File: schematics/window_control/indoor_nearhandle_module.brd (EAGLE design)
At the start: 54.6 x 59.4 mm, 19 parts, among them J1 J2, J2 J2, Q1 2N3904, SW1 MRS-101-2C3-B, U1 ESP32, U4 SN74LS32N

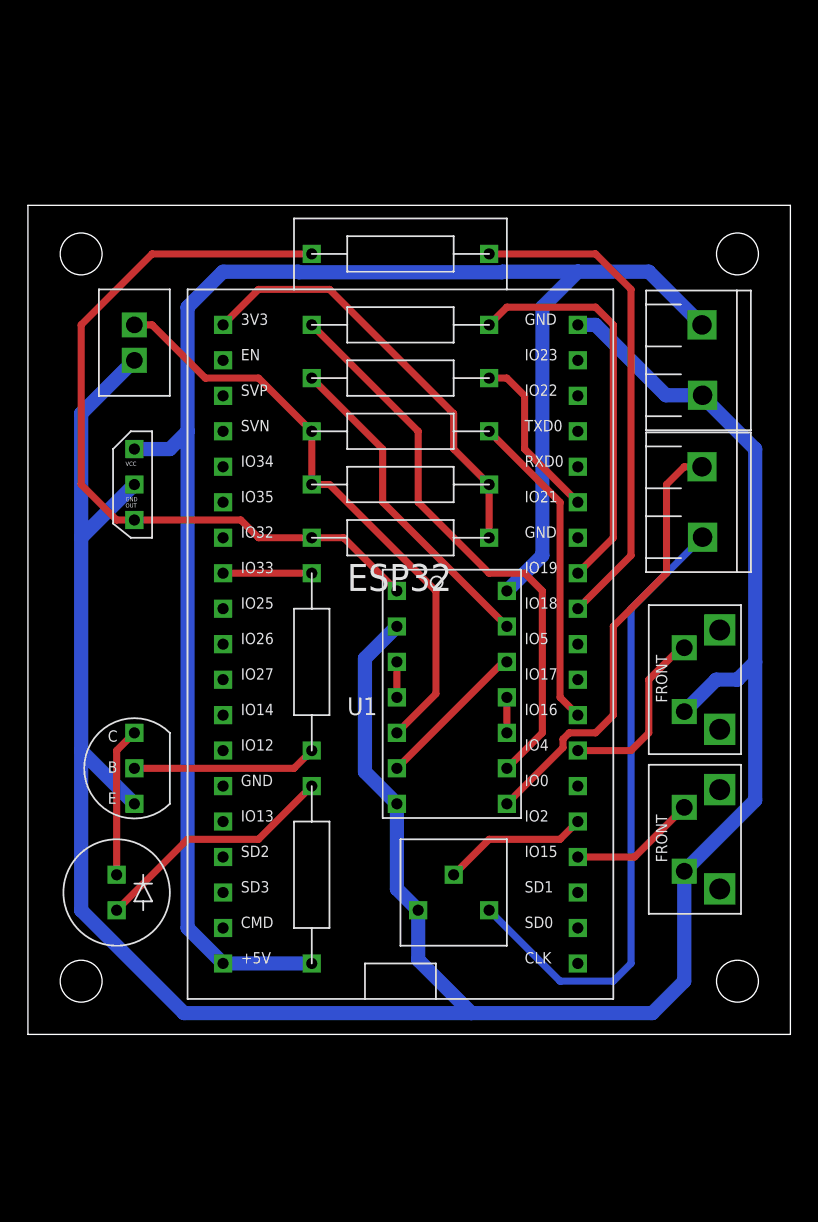
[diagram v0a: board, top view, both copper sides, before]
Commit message: Board redesigned to reduce it width
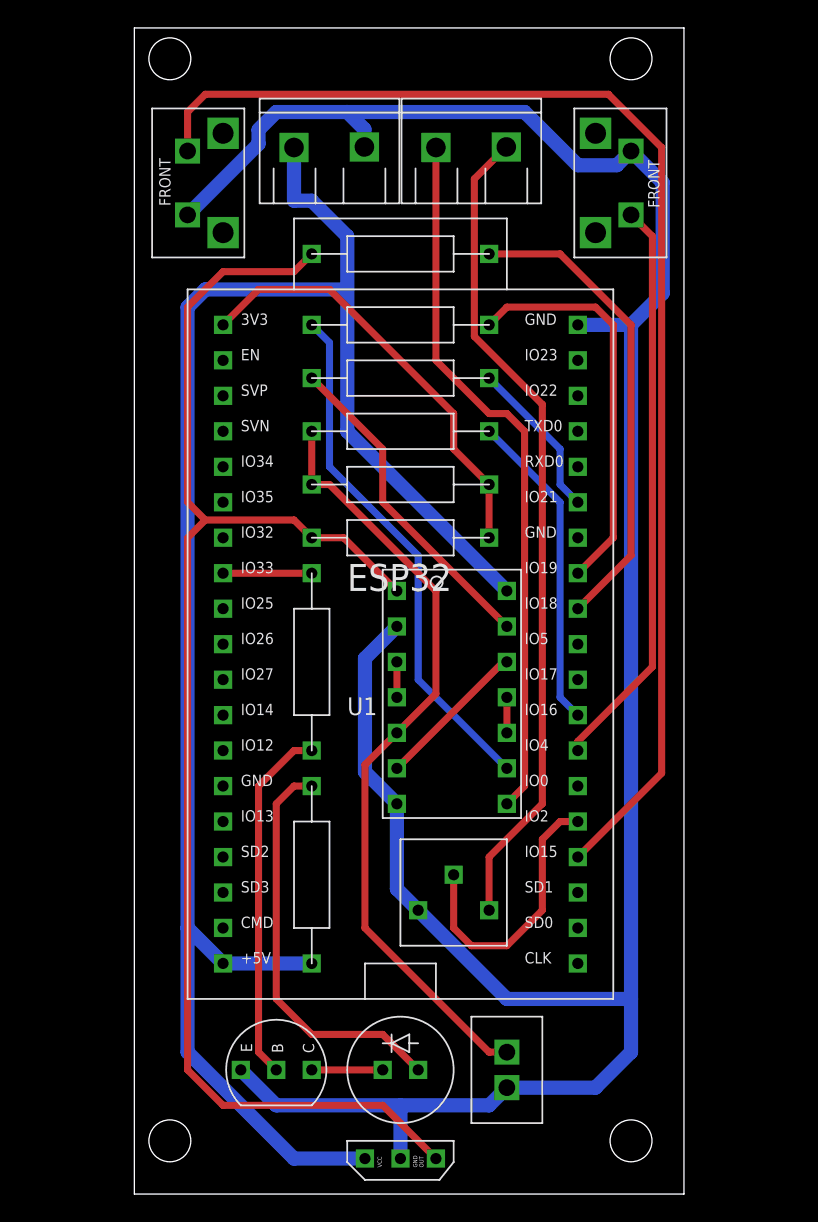
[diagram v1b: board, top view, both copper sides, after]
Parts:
- moved SB2 58.9 mm to (19.1, 67.3)
- moved SW1 58.5 mm to (41.9, 3.81)
- moved B1 51.9 mm to (34.3, -2.54), turned to 90 degrees
- moved SB1 35.8 mm to (50.8, 67.3), turned to 90 degrees
- moved J2 30.7 mm to (29.2, 69.8), turned to 90 degrees
- moved J1 30.3 mm to (39.4, 69.8), turned to 90 degrees
- moved D1 24.0 mm to (34.3, 3.81), turned to 180 degrees
- moved Q1 21.6 mm to (24.1, 5.08), turned to 270 degrees
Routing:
- net GPIO_TS_WINDOW_CLOSE: track 9.09 -> 92.1 mm
- net HALL_OUT_INV: track 55.8 -> 102.4 mm
- net GPIO_TS_WINDOW_OPEN: track 12.9 -> 41.2 mm
- net SERVO_PWM_CONTROL: track 31.8 -> 50.9 mm
- net OUTDOOR_SIGNAL: track 45.4 -> 59.2 mm
- net SW_IS_ON_INV: track 43.0 -> 55.9 mm
- net N$5: track 13.2 -> 25.7 mm
- net N$8: track 17.7 -> 29.3 mm
- net N$13: track 10.5 -> 19.9 mm
- net GND: track 193.9 -> 185.7 mm
- net +5V: track 123.2 -> 129.9 mm
- net N$7: track 10.7 -> 5.08 mm
- net SERVO_PWM: track 41.1 -> 37.5 mm
- net N$29: track 35.7 -> 34.2 mm
- net N$28: track 12.3 -> 11.5 mm
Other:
- board size 54.6 x 59.4 mm -> 39.4 x 83.5 mm

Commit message: Indoor board - ready
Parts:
- turned J1 to 270 degrees
- turned J2 to 270 degrees
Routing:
- net SERVO_PWM_CONTROL: track 50.9 -> 62.4 mm
- net N$8: track 29.3 -> 23.5 mm
- net N$5: track 25.7 -> 23.9 mm
- net +5V: track 129.9 -> 128.1 mm
- net OUTDOOR_SIGNAL: track 59.2 -> 59.8 mm
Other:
- board text added: "+5V"
- board text added: "B1"
- board text added: "D1"
- board text added: "GND"
- board text added: "J1"
- board text added: "J2"
- board text added: "OUT_SGN"
- board text added: "Q1"
- board text added: "R1"
- board text added: "R12"
- board text added: "R13"
- board text added: "R2"
- board text added: "R4"
- board text added: "R5"
- board text added: "R6"
- board text added: "R7"
- board text added: "R8"
- board text added: "SB1"
- board text added: "SB2"
- board text added: "SRV_PWM"
- board text added: "SW1"
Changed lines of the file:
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@@
 <hole x="17.78" y="-1.27" drill="3"/>
 <hole x="50.8" y="-1.27" drill="3"/>
+<text x="16.51" y="73.66" size="0.8128" layer="25">SB2</text>
+<text x="50.8" y="73.66" size="0.8128" layer="25">SB1</text>
+<text x="24.13" y="63.5" size="1.778" layer="25">J2</text>
+<text x="43.18" y="63.5" size="1.778" layer="25">J1</text>
+<text x="38.1" y="59.69" size="1.778" layer="25">R8</text>
+<text x="27.94" y="58.42" size="1.778" layer="25">R5</text>
+<text x="38.1" y="54.61" size="1.778" layer="25">R7</text>
+<text x="26.67" y="50.8" size="1.778" layer="25">R4</text>
+<text x="38.1" y="46.99" size="1.778" layer="25">R12</text>
+<text x="26.67" y="43.18" size="1.778" layer="25">R13</text>
+<text x="29.21" y="35.56" size="1.778" layer="25">R1</text>
+<text x="29.21" y="20.32" size="1.778" layer="25">R2</text>
+<text x="39.37" y="10.16" size="1.778" layer="25">R6</text>
+<text x="19.05" y="6.35" size="1.778" layer="25">Q1</text>
+<text x="27.94" y="6.35" size="1.778" layer="25">D1</text>
+<text x="44.45" y="6.35" size="1.778" layer="25">SW1</text>
+<text x="39.37" y="-2.54" size="1.778" layer="25">B1</text>
+<text x="29.21" y="66.04" size="1.778" layer="26" rot="MR0">GND</text>
+<text x="33.02" y="72.39" size="1.778" layer="26" rot="MR0">+5V</text>
+<text x="43.18" y="66.04" size="1.778" layer="26" rot="MR0">OUT_SGN</text>
+<text x="48.26" y="72.39" size="1.778" layer="26" rot="MR0">SRV_PWM</text>
 </plain>
 <attributes>
@@
 <element name="B1" library="my_devices" package="HALL_SENSOR" value="A3144" x="34.29" y="-2.54" smashed="yes" rot="R90"/>
 <element name="D1" library="my_devices" package="LD" value="GNL-3014ED" x="34.29" y="3.81" smashed="yes" rot="R180"/>
-<element name="J1" library="my_devices" package="J2" value="J2" x="39.37" y="69.85" smashed="yes" rot="R90"/>
-<element name="J2" library="my_devices" package="J2" value="J2" x="29.21" y="69.85" smashed="yes" rot="R90"/>
+<element name="J1" library="my_devices" package="J2" value="J2" x="39.37" y="69.85" smashed="yes" rot="R270"/>
+<element name="J2" library="my_devices" package="J2" value="J2" x="29.21" y="69.85" smashed="yes" rot="R270"/>
 <element name="Q1" library="my_devices" package="TRANSISTOR" value="2N3904" x="24.13" y="5.08" smashed="yes" rot="R270"/>
 <element name="R1" library="my_devices" package="R" value="620" x="27.94" y="33.02" smashed="yes" rot="R270">
@@
 <wire x1="19.05" y1="13.97" x2="21.59" y2="11.43" width="1.016" layer="16"/>
 <wire x1="21.59" y1="11.43" x2="27.94" y2="11.43" width="1.016" layer="16"/>
-<wire x1="26.67" y1="66.04" x2="26.67" y2="69.85" width="1.016" layer="16"/>
 <wire x1="41.91" y1="38.1" x2="30.48" y2="49.53" width="1.016" layer="16"/>
 <wire x1="30.48" y1="49.53" x2="30.48" y2="59.69" width="1.016" layer="16"/>
-<wire x1="30.48" y1="59.69" x2="30.48" y2="63.5" width="1.016" layer="16"/>
-<wire x1="30.48" y1="63.5" x2="27.94" y2="66.04" width="1.016" layer="16"/>
-<wire x1="27.94" y1="66.04" x2="26.67" y2="66.04" width="1.016" layer="16"/>
+<wire x1="30.48" y1="59.69" x2="30.48" y2="62.23" width="1.016" layer="16"/>
+<wire x1="30.48" y1="62.23" x2="30.48" y2="63.5" width="1.016" layer="16"/>
 <wire x1="31.75" y1="-2.54" x2="26.67" y2="-2.54" width="1.016" layer="16"/>
 <wire x1="26.67" y1="-2.54" x2="19.05" y2="5.08" width="1.016" layer="16"/>
@@
 <wire x1="19.05" y1="58.42" x2="20.32" y2="59.69" width="1.016" layer="16"/>
 <wire x1="20.32" y1="59.69" x2="30.48" y2="59.69" width="1.016" layer="16"/>
+<wire x1="30.48" y1="63.5" x2="30.48" y2="68.58" width="1.016" layer="16"/>
+<wire x1="30.48" y1="68.58" x2="31.75" y2="69.85" width="1.016" layer="16"/>
 </signal>
 <signal name="GND">
@@
 <wire x1="34.29" y1="1.27" x2="34.29" y2="-2.54" width="1.016" layer="16"/>
 <wire x1="19.05" y1="65.024" x2="24.13" y2="70.104" width="1.016" layer="16"/>
-<wire x1="24.13" y1="70.104" x2="24.13" y2="71.12" width="1.016" layer="16"/>
+<wire x1="24.13" y1="71.12" x2="24.13" y2="70.104" width="1.016" layer="16"/>
 <wire x1="24.13" y1="71.12" x2="25.4" y2="72.39" width="1.016" layer="16"/>
-<wire x1="31.71" y1="71.16" x2="30.48" y2="72.39" width="1.016" layer="16"/>
-<wire x1="31.71" y1="71.16" x2="31.71" y2="69.89" width="1.016" layer="16"/>
-<wire x1="25.4" y1="72.39" x2="30.48" y2="72.39" width="1.016" layer="16"/>
-<wire x1="30.48" y1="72.39" x2="43.18" y2="72.39" width="1.016" layer="16"/>
+<wire x1="25.4" y1="72.39" x2="43.18" y2="72.39" width="1.016" layer="16"/>
 <wire x1="43.18" y1="72.39" x2="46.99" y2="68.58" width="1.016" layer="16"/>
 <wire x1="46.99" y1="68.58" x2="49.784" y2="68.58" width="1.016" layer="16"/>
@@
 <wire x1="53.066" y1="59.416" x2="50.8" y2="57.15" width="1.016" layer="16"/>
 <wire x1="53.066" y1="67.33" x2="53.066" y2="59.416" width="1.016" layer="16"/>
+<wire x1="24.13" y1="70.104" x2="24.424" y2="69.81" width="1.016" layer="16"/>
+<wire x1="24.424" y1="69.81" x2="26.71" y2="69.81" width="1.016" layer="16"/>
 </signal>
 <signal name="GPIO_TS_WINDOW_OPEN">
@@
 <wire x1="43.18" y1="49.53" x2="41.91" y2="50.8" width="0.508" layer="1"/>
 <wire x1="41.91" y1="50.8" x2="40.64" y2="50.8" width="0.508" layer="1"/>
-<wire x1="40.64" y1="50.8" x2="36.83" y2="54.61" width="0.508" layer="1"/>
-<wire x1="36.83" y1="54.61" x2="36.83" y2="69.85" width="0.508" layer="1"/>
 <wire x1="43.18" y1="24.13" x2="43.18" y2="49.53" width="0.508" layer="1"/>
+<wire x1="34.29" y1="71.12" x2="35.56" y2="72.39" width="0.508" layer="1"/>
+<wire x1="35.56" y1="72.39" x2="39.37" y2="72.39" width="0.508" layer="1"/>
+<wire x1="39.37" y1="72.39" x2="41.91" y2="69.85" width="0.508" layer="1"/>
+<wire x1="40.64" y1="50.8" x2="34.29" y2="57.15" width="0.508" layer="1"/>
+<wire x1="34.29" y1="57.15" x2="34.29" y2="71.12" width="0.508" layer="1"/>
 </signal>
 <signal name="N$3">
@@
 <contactref element="R1" pad="P$2"/>
 <contactref element="Q1" pad="B"/>
-<wire x1="25.4" y1="3.81" x2="24.13" y2="5.08" width="0.508" layer="1"/>
-<wire x1="24.13" y1="5.08" x2="24.13" y2="24.13" width="0.508" layer="1"/>
-<wire x1="24.13" y1="24.13" x2="26.67" y2="26.67" width="0.508" layer="1"/>
-<wire x1="26.67" y1="26.67" x2="27.94" y2="26.67" width="0.508" layer="1"/>
+<wire x1="25.4" y1="3.81" x2="25.4" y2="24.13" width="0.508" layer="1"/>
+<wire x1="25.4" y1="24.13" x2="27.94" y2="26.67" width="0.508" layer="1"/>
 </signal>
 <signal name="N$7">
@@
 <contactref element="D1" pad="PIN_CATHODE"/>
 <contactref element="R2" pad="P$1"/>
-<wire x1="25.4" y1="8.89" x2="27.94" y2="6.35" width="0.508" layer="1"/>
-<wire x1="25.4" y1="8.89" x2="25.4" y2="22.86" width="0.508" layer="1"/>
-<wire x1="25.4" y1="22.86" x2="26.67" y2="24.13" width="0.508" layer="1"/>
-<wire x1="26.67" y1="24.13" x2="27.94" y2="24.13" width="0.508" layer="1"/>
-<wire x1="27.94" y1="6.35" x2="33.02" y2="6.35" width="0.508" layer="1"/>
-<wire x1="33.02" y1="6.35" x2="35.56" y2="3.81" width="0.508" layer="1"/>
+<wire x1="35.56" y1="3.81" x2="30.48" y2="8.89" width="0.508" layer="1"/>
+<wire x1="30.48" y1="21.59" x2="27.94" y2="24.13" width="0.508" layer="1"/>
+<wire x1="30.48" y1="8.89" x2="30.48" y2="21.59" width="0.508" layer="1"/>
 </signal>
 <signal name="LED_CONTROL">
@@
 <contactref element="J1" pad="PIN_2"/>
 <contactref element="R6" pad="P2"/>
-<wire x1="44.45" y1="51.4572625" x2="39.5796" y2="56.3276625" width="0.508" layer="1"/>
-<wire x1="39.5796" y1="67.5996" x2="41.87" y2="69.89" width="0.508" layer="1"/>
-<wire x1="39.5796" y1="56.3276625" x2="39.5796" y2="67.5996" width="0.508" layer="1"/>
+<wire x1="44.45" y1="51.4572625" x2="38.42863125" y2="57.47863125" width="0.508" layer="1"/>
+<wire x1="38.42863125" y1="57.47863125" x2="38.1" y2="57.8072625" width="0.508" layer="1"/>
 <wire x1="40.64" y1="15.24" x2="40.64" y2="19.05" width="0.508" layer="1"/>
 <wire x1="44.45" y1="22.86" x2="44.45" y2="51.4572625" width="0.508" layer="1"/>
 <wire x1="40.64" y1="19.05" x2="44.45" y2="22.86" width="0.508" layer="1"/>
+<wire x1="38.42863125" y1="57.47863125" x2="38.42863125" y2="68.25136875" width="0.508" layer="1"/>
+<wire x1="38.42863125" y1="68.25136875" x2="36.87" y2="69.81" width="0.508" layer="1"/>
 </signal>
 <signal name="N$6">
